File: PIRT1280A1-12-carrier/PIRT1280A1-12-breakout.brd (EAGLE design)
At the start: 76.2 x 68.6 mm, 39 parts, among them U1 PIRT1280A1-12

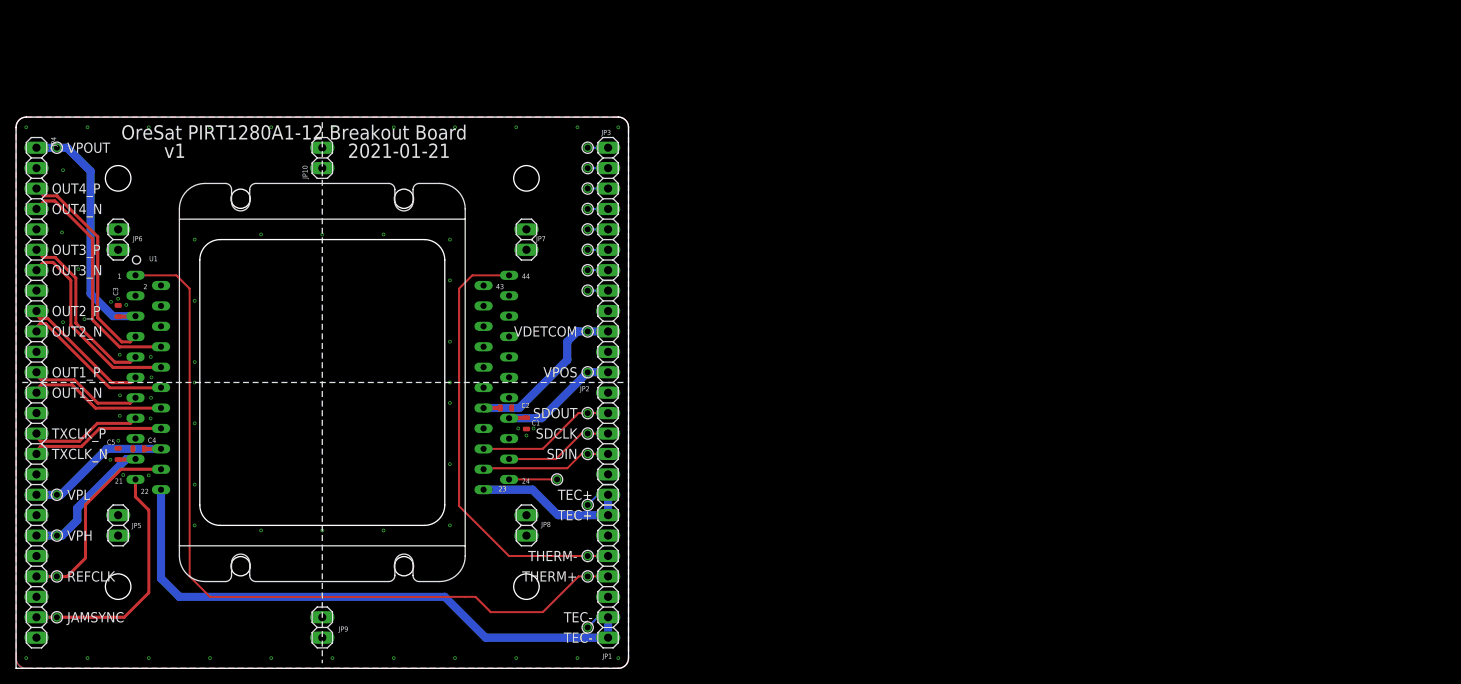
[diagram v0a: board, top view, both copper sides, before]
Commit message: Prototype of PIRT sensor and an example LT3042 power supply layout for one of the supplies.
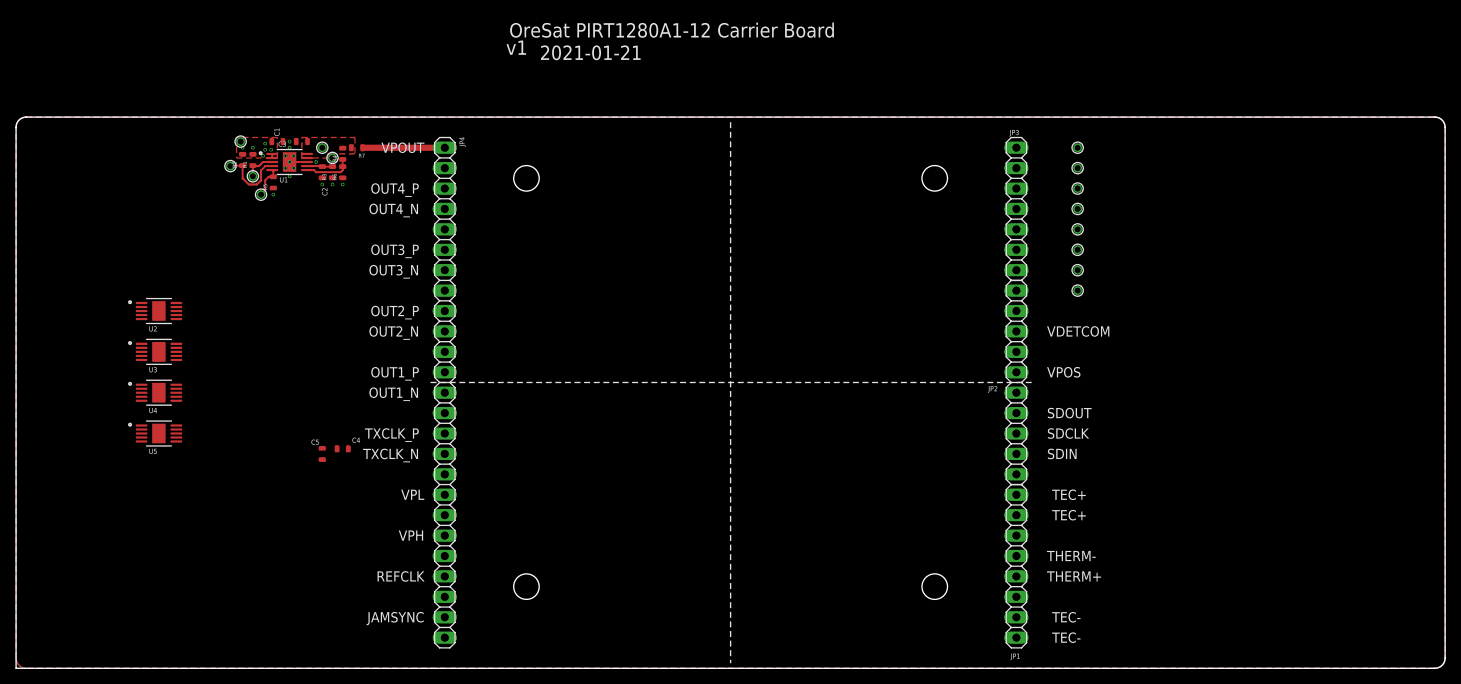
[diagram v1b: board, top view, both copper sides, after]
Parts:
- removed JP10, JP5, JP6, JP7, JP8, JP9: (no value), pinhead:1X02
- removed TP15, TP16, TP17, TP18, TP19, TP20, TP21, TP22, TP23: TEST-POINT-LARGE-SQUARE, oresat-misc:1X01
- added R1, R2: 10k, oresat-rcl:.0603-C-NOSILK
- added R3, R4, R5, R6: (no value), oresat-rcl:.0603-C-NOSILK
- added R7: 0, oresat-rcl:.0603-C-NOSILK
- added U2, U3, U4, U5: LT3042IMSE#TRPBF, U-Analog-LT3042-ultralow-noise-ldo:SOP50P490X110-11N
- C1, C2, C3: value 100n -> 4.7u
- U1: value PIRT1280A1-12 -> LT3042IMSE#TRPBF; device PIRT1280A1-12:PIRT1280A1-12 -> U-Analog-LT3042-ultralow-noise-ldo:SOP50P490X110-11N
- moved TP13 68.2 mm to (38.1, 64.8)
- moved TP2 61.0 mm to (132.1, 47.0)
- moved TP3 61.0 mm to (132.1, 49.5)
- moved TP4 61.0 mm to (132.1, 52.1)
- moved TP5 61.0 mm to (132.1, 54.6)
- moved TP6 61.0 mm to (132.1, 57.1)
- moved TP7 61.0 mm to (132.1, 59.7)
- moved TP8 61.0 mm to (132.1, 62.2)
- moved TP9 61.0 mm to (132.1, 64.8)
- moved TP14 56.1 mm to (30.5, 58.9), turned to 180 degrees
- moved TP10 55.5 mm to (26.7, 62.5), turned to 180 degrees
- moved TP12 54.8 mm to (27.9, 65.5), turned to 180 degrees
- moved TP11 54.1 mm to (29.5, 61.2), turned to 180 degrees
- moved JP4 50.8 mm to (53.3, 35.6)
- moved JP1 50.8 mm to (124.5, 12.7)
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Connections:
- removed net ABITOUT: TP1.1, U1.24
- new net 5V: C1.1, R1.2, R2.2, TP12.1, U1.1, U1.2
- new net IN: U2.1, U2.2, U3.1, U3.2, U4.1, U4.2, U5.1, U5.2
- new net N$10: C2.1, R3.2, TP1.1, U1.7
- new net N$11: R2.1, TP10.1, U1.4
- new net N$12: R5.2, TP14.1, U1.5
- new net N$15: R4.1, R6.2, U1.6
- new net N$9: R1.1, TP11.1, U1.3
- new net OUT: U2.10, U3.10, U4.10, U5.10
- new net OUTS: U2.9, U3.9, U4.9, U5.9
- new net VPOUT: C3.1, R4.2, R7.2, TP13.1, U1.10, U1.9
- net GND: now also R3.1, R5.1, R6.1, U1.11, U1.8, U2.11, U2.8, U3.11, U3.8, U4.11, U4.8, U5.11, U5.8; no longer C4.2, C5.2, JP10.1, JP10.2, JP5.1, JP5.2, JP6.1, JP6.2, JP7.1, JP7.2, JP8.1, JP8.2, JP9.1, JP9.2, U1.17, U1.29, U1.6
- net JAMSYNC: no longer TP19.1, U1.21
- net OUT1_N: no longer U1.14
- net OUT1_P: no longer U1.13
- net OUT2_N: no longer U1.12
- net OUT2_P: no longer U1.11
- net OUT3_N: no longer U1.10
- net OUT3_P: no longer U1.9
- net OUT4_N: no longer U1.8
- net OUT4_P: no longer U1.7
- net REFCLK: no longer TP20.1, U1.20
- net SDCLK: no longer TP10.1, U1.26
- net SDIN: no longer TP11.1, U1.25
- net SDOUT: no longer TP12.1, U1.27
- net TEC+: no longer TP14.1, U1.23
- net TEC-: no longer TP13.1, U1.22
- net THERM+: no longer TP15.1, U1.1
- net THERM-: no longer TP16.1, U1.44
- net TXCLK_N: no longer U1.16
- net TXCLK_P: no longer U1.15
- net VEDETCOM-2.9V: no longer C2.1, TP17.1, U1.31
- net VPH-3.3V: no longer C5.1, TP21.1, U1.19
- net VPL-1.6V: no longer C4.1, TP22.1, U1.18
- net VPOS-3.3V: no longer C1.1, TP18.1, U1.30
- net VPOUT-0.9V: now also R7.1; no longer C3.1, TP23.1, U1.5
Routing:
- net THERM+: track 99.0 -> 0.00 mm
- net TEC-: track 75.3 -> 0.00 mm
- net THERM-: track 55.1 -> 0.00 mm
- net JAMSYNC: track 30.0 -> 0.00 mm
- net OUT4_N: track 29.3 -> 0.00 mm
- net OUT4_P: track 26.4 -> 0.00 mm
- net REFCLK: track 24.9 -> 0.00 mm
- net OUT3_N: track 24.7 -> 0.00 mm
- net VEDETCOM-2.9V: track 22.9 -> 0.00 mm
- net TEC+: track 22.4 -> 0.00 mm
- net VPOUT-0.9V: track 32.1 -> 10.2 mm
- net OUT3_P: track 21.7 -> 0.00 mm
- net VPL-1.6V: track 20.0 -> 0.00 mm
- net OUT2_N: track 19.5 -> 0.00 mm
- net VPH-3.3V: track 19.3 -> 0.00 mm
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- added copper zone on layer 1, net 5V
- added copper zone on layer 1, net VPOUT
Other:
- board size 76.2 x 68.6 mm -> 177.8 x 68.6 mm
- board text added: "OreSat PIRT1280A1-12 Carrier Board"
- board text removed: "OreSat PIRT1280A1-12 Breakout Board"
